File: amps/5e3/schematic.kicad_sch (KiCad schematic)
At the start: 44 parts, among them T2 8k:8

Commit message: Add: real tube pin numbers and readable valve glyphs on every schematic
Phase B of the drawing program. A factory service sheet numbers every tube
pin, because the number is what a technician puts a probe on. This corpus
printed none, and the numbers hidden in its symbols were positional
placeholders (P=1, G=2, K=3) that would have published a 6V6GT's plate as
pin 1 when it is pin 3.

1055 electrodes now carry the real number, 1027 lettered (27 are shared
filaments deduped, 1 dropped for want of clear space on the 6G2). Resolved per
instance from reference/tubes/<slug>.yaml through the same alias resolution the
layout renderer uses, so a 12AX7 section and a 6SL7 section each get their own
basing. A valve whose basing the corpus does not carry prints nothing rather
than a wrong number.

Section letters and basing units are now separate things, which cost a detour
worth recording. The RCA 12AX7-A sheet reads "Pin 1 - Plate of Unit No.2 ...
Pin 6 - Plate of Unit No.1", so unit numbering is not pin order; the 5Y3 and
GZ34 number their units in opposite pin order, so nothing positional can
express it. But the section LETTER is a designator, not a basing fact: this
corpus, like every technician, calls the first stage in signal order V1A, and
five amps' prose already did. On four amps the factory sheets put that first
stage on the other half -- the AA764's own schematic prints +200 V on pin 1 --
so those drawings now state their unit explicitly, each citing its source, and
no letter, netlist, parts list or layout comment changed. 183 layout comments
agree with the printed numbers, 0 disagree. A guard fires if two halves of one
bottle resolve to the same unit, which is exactly how this was found.

Glyphs: the cathode gains a bracket and filament hairpin so it can no longer be
confused with the plate bar, the pentode's screen sits on its own row, and a
rectifier draws as one envelope over its sections instead of two apparent
bottles. Line weights are scaled per sheet to a co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
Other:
- note added: "1"
- note added: "2"
- note added: "2,8"
- note added: "3"
- note added: "4"
- note added: "5"
- note added: "6"
- note added: "7"
- note added: "8"
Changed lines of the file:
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@@
   (wire (pts (xy 29.7916 38.278) (xy 33.6016 38.278))
     (stroke (width 0) (type default)))
-  (junction (at 29.7916 38.278) (diameter 0) (color 0 0 0 0))
+  (junction (at 29.7916 38.278) (diameter 1) (color 0 0 0 0))
   (symbol (lib_id "cx:R") (at 29.7916 42.088 0) (unit 1)
     (in_bom yes) (on_board yes)
@@
   (wire (pts (xy 29.7916 70.278) (xy 33.6016 70.278))
     (stroke (width 0) (type default)))
-  (junction (at 29.7916 70.278) (diameter 0) (color 0 0 0 0))
+  (junction (at 29.7916 70.278) (diameter 1) (color 0 0 0 0))
   (symbol (lib_id "cx:R") (at 29.7916 74.088 0) (unit 1)
     (in_bom yes) (on_board yes)
@@
   (wire (pts (xy 48.8416 80.278) (xy 48.8416 83.278))
     (stroke (width 0) (type default)))
-  (junction (at 48.8416 80.278) (diameter 0) (color 0 0 0 0))
+  (junction (at 48.8416 80.278) (diameter 1) (color 0 0 0 0))
   (symbol (lib_id "cx:R") (at 48.8416 87.088 0) (unit 1)
     (in_bom yes) (on_board yes)
@@
   (wire (pts (xy 41.2216 30.658) (xy 53.9216 30.658))
     (stroke (width 0) (type default)))
-  (junction (at 41.2216 30.658) (diameter 0) (color 0 0 0 0))
+  (junction (at 41.2216 30.658) (diameter 1) (color 0 0 0 0))
   (symbol (lib_id "cx:C") (at 57.7316 30.658 90) (unit 1)
     (in_bom yes) (on_board yes)
@@
   (wire (pts (xy 41.2216 62.658) (xy 53.9216 62.658))
     (stroke (width 0) (type default)))
-  (junction (at 41.2216 62.658) (diameter 0) (color 0 0 0 0))
+  (junction (at 41.2216 62.658) (diameter 1) (color 0 0 0 0))
   (symbol (lib_id "cx:C") (at 57.7316 62.658 90) (unit 1)
     (in_bom yes) (on_board yes)
@@
   (wire (pts (xy 74.2416 66.468) (xy 74.2416 50.278))
     (stroke (width 0) (type default)))
-  (junction (at 74.2416 50.278) (diameter 0) (color 0 0 0 0))
+  (junction (at 74.2416 50.278) (diameter 1) (color 0 0 0 0))
   (symbol (lib_id "cx:TRIODE") (at 84.4016 50.278 0) (unit 1)
     (in_bom yes) (on_board yes)
@@
   (wire (pts (xy 84.4016 42.658) (xy 94.5616 42.658))
     (stroke (width 0) (type default)))
-  (junction (at 84.4016 42.658) (diameter 0) (color 0 0 0 0))
+  (junction (at 84.4016 42.658) (diameter 1) (color 0 0 0 0))
   (wire (pts (xy 94.5616 42.658) (xy 94.5616 35.178))
     (stroke (width 0) (type default)))
@@
     (property "Reference" "RKA" (at 128.512 64.808 0) (effects (font (size 1.27 1.27)) (justify left)))
     (property "Value" "1.5k" (at 128.512 67.208 0) (effects (font (size 1.27 1.27)) (justify left))))
-  (junction (at 126.312 71.818) (diameter 0) (color 0 0 0 0))
+  (junction (at 126.312 71.818) (diameter 1) (color 0 0 0 0))
   (symbol (lib_id "cx:R") (at 126.312 75.628 0) (unit 1)
     (in_bom yes) (on_board yes)
@@
   (wire (pts (xy 116.152 54.278) (xy 116.152 64.198))
     (stroke (width 0) (type default)))
-  (junction (at 116.152 54.278) (diameter 0) (color 0 0 0 0))
+  (junction (at 116.152 54.278) (diameter 1) (color 0 0 0 0))
   (symbol (lib_id "cx:R") (at 116.152 68.008 0) (unit 1)
     (in_bom yes) (on_board yes)
@@
   (wire (pts (xy 126.312 46.658) (xy 133.932 46.658))
     (stroke (width 0) (type default)))
-  (junction (at 126.312 46.658) (diameter 0) (color 0 0 0 0))
+  (junction (at 126.312 46.658) (diameter 1) (color 0 0 0 0))
   (wire (pts (xy 141.552 46.658) (xy 142.882 46.658))
     (stroke (width 0) (type default)))
@@
   (wire (pts (xy 155.522 34.278) (xy 155.522 34.278))
     (stroke (width 0) (type default)))
-  (junction (at 146.632 34.278) (diameter 0) (color 0 0 0 0))
+  (junction (at 146.632 34.278) (diameter 1) (color 0 0 0 0))
   (symbol (lib_id "cx:R") (at 146.632 38.088 0) (unit 1)
     (in_bom yes) (on_board yes)
@@
   (wire (pts (xy 155.522 74.278) (xy 155.522 74.278))
     (stroke (width 0) (type default)))
-  (junction (at 146.632 74.278) (diameter 0) (color 0 0 0 0))
+  (junction (at 146.632 74.278) (diameter 1) (color 0 0 0 0))
   (symbol (lib_id "cx:R") (at 146.632 78.088 0) (unit 1)
     (in_bom yes) (on_board yes)
@@
   (wire (pts (xy 179.652 84.278) (xy 179.652 88.278))
     (stroke (width 0) (type default)))
-  (junction (at 179.652 84.278) (diameter 0) (color 0 0 0 0))
+  (junction (at 179.652 84.278) (diameter 1) (color 0 0 0 0))
   (symbol (lib_id "cx:R") (at 179.652 92.088 0) (unit 1)
     (in_bom yes) (on_board yes)
@@
   (wire (pts (xy 59.0016 120.078) (xy 78.0516 120.078))
     (stroke (width 0) (type default)))
-  (junction (at 46.3016 120.078) (diameter 0) (color 0 0 0 0))
-  (junction (at 59.0016 120.078) (diameter 0) (color 0 0 0 0))
+  (junction (at 46.3016 120.078) (diameter 1) (color 0 0 0 0))
+  (junction (at 59.0016 120.078) (diameter 1) (color 0 0 0 0))
   (symbol (lib_id "cx:C") (at 59.0016 123.888 0) (unit 1)
     (in_bom yes) (on_board yes)
@@
   (wire (pts (xy 94.5616 120.078) (xy 97.1016 120.078))
     (stroke (width 0) (type default)))
-  (junction (at 90.7516 120.078) (diameter 0) (color 0 0 0 0))
+  (junction (at 90.7516 120.078) (diameter 1) (color 0 0 0 0))
   (global_label "B+2" (shape input) (at 90.7516 117.538 90)
     (effects (font (size 1.27 1.27)) (justify left)))
   (wire (pts (xy 90.7516 117.538) (xy 90.7516 120.078))
     (stroke (width 0) (type default)))
-  (junction (at 94.5616 120.078) (diameter 0) (color 0 0 0 0))
+  (junction (at 94.5616 120.078) (diameter 1) (color 0 0 0 0))
   (symbol (lib_id "cx:C") (at 94.5616 123.888 0) (unit 1)
     (in_bom yes) (on_board yes)
@@
   (wire (pts (xy 107.262 120.078) (xy 112.342 120.078))
     (stroke (width 0) (type default)))
-  (junction (at 107.262 120.078) (diameter 0) (color 0 0 0 0))
+  (junction (at 107.262 120.078) (diameter 1) (color 0 0 0 0))
   (global_label "B+3" (shape input) (at 107.262 117.538 90)
     (effects (font (size 1.27 1.27)) (justify left)))
@@
   (global_label "GND" (shape input) (at 112.342 127.698 270)
     (effects (font (size 1.27 1.27)) (justify right)))
+  (polyline (pts (xy 46.3016 104.978) (xy 47.2926 105.076) (xy 48.2456 105.365) (xy 49.1236 105.834) (xy 49.8936 106.466) (xy 50.5256 107.236) (xy 50.9946 108.114) (xy 51.2836 109.067) (xy 51.3816 110.058) (xy 51.2836 111.049) (xy 50.9946 112.002) (xy 50.5256 112.88) (xy 49.8936 113.65) (xy 49.1236 114.282) (xy 48.2456 114.751) (xy 47.2926 115.04) (xy 46.3016 115.138) (xy 33.6016 115.138) (xy 32.6106 115.04) (xy 31.6576 114.751) (xy 30.7796 114.282) (xy 30.0096 113.65) (xy 29.3776 112.88) (xy 28.9086 112.002) (xy 28.6196 111.049) (xy 28.5216 110.058) (xy 28.6196 109.067) (xy 28.9086 108.114) (xy 29.3776 107.236) (xy 30.0096 106.466) (xy 30.7796 105.834) (xy 31.6576 105.365) (xy 32.6106 105.076) (xy 33.6016 104.978) (xy 46.3016 104.978))
+    (stroke (width 0.3) (type default) (color 197 163 255 1)) (fill (type none)))
+  (polyline (pts (xy 31.7016 112.293) (xy 33.6016 110.693) (xy 39.9516 112.773) (xy 46.3016 110.693) (xy 48.2016 112.293))
+    (stroke (width 0.3) (type default) (color 197 163 255 1)) (fill (type none)))
+  (text "6" (at 42.0716 31.928 0)
+    (effects (font (size 1.1 1.1)) (justify left)))
+  (text "7" (at 34.2744 36.878 0)
+    (effects (font (size 1.1 1.1)) (justify left)))
+  (text "8" (at 43.5216 44.628 0)
+    (effects (font (size 1.1 1.1)) (justify left)))
+  (text "1" (at 42.0716 63.928 0)
+    (effects (font (size 1.1 1.1)) (justify left)))
+  (text "2" (at 34.2744 68.878 0)
+    (effects (font (size 1.1 1.1)) (justify left)))
+  (text "3" (at 42.0716 76.628 0)
+    (effects (font (size 1.1 1.1)) (justify left)))
+  (text "6" (at 85.2516 43.928 0)
+    (effects (font (size 1.1 1.1)) (justify left)))
+  (text "7" (at 77.4544 48.878 0)
+    (effects (font (size 1.1 1.1)) (justify left)))
+  (text "8" (at 85.2516 56.628 0)
+    (effects (font (size 1.1 1.1)) (justify left)))
+  (text "1" (at 127.162 47.928 0)
+    (effects (font (size 1.1 1.1)) (justify left)))
+  (text "2" (at 119.364 52.878 0)
+    (effects (font (size 1.1 1.1)) (justify left)))
+  (text "3" (at 127.162 60.628 0)
+    (effects (font (size 1.1 1.1)) (justify left)))
+  (text "3" (at 163.992 27.293 0)
+    (effects (font (size 1.1 1.1)) (justify left)))
+  (text "5" (at 156.194 32.878 0)
+    (effects (font (size 1.1 1.1)) (justify left)))
+  (text "4" (at 169.042 31.608 0)
+    (effects (font (size 1.1 1.1)) (justify left)))
+  (text "8" (at 163.992 39.993 0)
+    (effects (font (size 1.1 1.1)) (justify left)))
+  (text "3" (at 163.992 67.293 0)
+    (effects (font (size 1.1 1.1)) (justify left)))
+  (text "5" (at 156.194 72.878 0)
+    (effects (font (size 1.1 1.1)) (justify left)))
+  (text "4" (at 169.042 71.608 0)
+    (effects (font (size 1.1 1.1)) (justify left)))
+  (text "8" (at 163.992 79.993 0)
+    (effects (font (size 1.1 1.1)) (justify left)))
+  (text "6" (at 34.4516 103.708 0)
+    (effects (font (size 1.1 1.1)) (justify left)))
+  (text "2,8" (at 34.4516 116.408 0)
+    (effects (font (size 1.1 1.1)) (justify left)))
+  (text "4" (at 47.1516 103.708 0)
+    (effects (font (size 1.1 1.1)) (justify left)))
   (text "Heaters and PT primary omitted — see netlist.cir and meta.yaml" (at 12.7 138.856 0)
     (effects (font (size 1.2 1.2)) (justify left)))

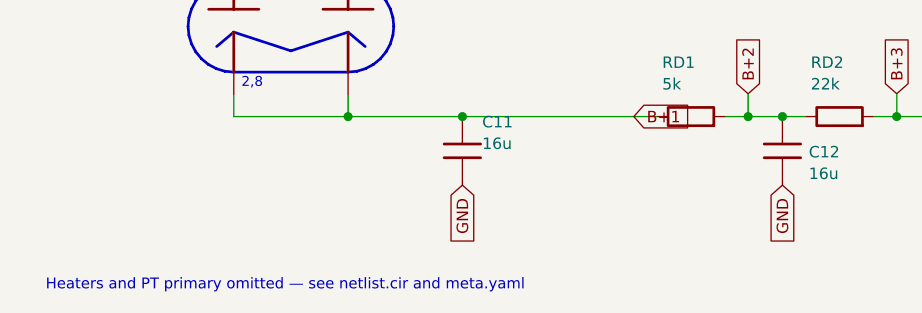
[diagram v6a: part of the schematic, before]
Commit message: Fix: schematic sheet notes no longer name repository files
Thirty-seven committed sheets rendered footnotes and section notes such as
"Heaters and PT primary omitted — see netlist.cir and meta.yaml" or
"excluded from netlist.cir (notes.md)" to visitors through KiCanvas. The
prose sweeps never counted sheets. Rewritten in the site's own words — the
netlist, the sources list, the circuit story, the parts list, the board
drawing — in 59 strings across 33 draw scripts, keeping every technical
claim as it was; the three tone sheets (6G4, 6G5, 6G6-B) are under repair
elsewhere and keep theirs for now. The sweep touched only strings passed to
the sheet's note, text, caption and footnote calls, never a path or a value.

Gates: check_schematics 40/0, connectivity 0 isolated pins;
verify_schematic_nets 40 clean; only the regenerated sheets and their served
copies changed.

Co-Authored-By: Claude Fable 5.1 <noreply@anthropic.com>
Claude-Session: https://claude.ai/code/session_01KBMfdh37HmCL2iWcBiL5J1
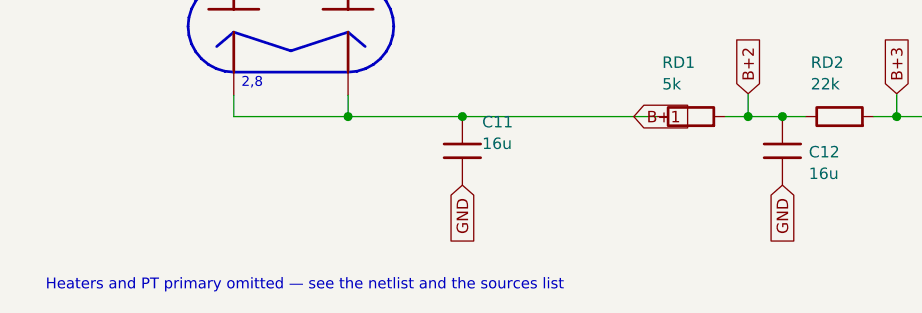
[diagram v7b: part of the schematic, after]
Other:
- note added: "Heaters and PT primary omitted — see the netlist and the sources list"
- note removed: "Heaters and PT primary omitted — see netlist.cir and meta.yaml"
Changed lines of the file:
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@@
   (text "4" (at 47.1516 103.708 0)
     (effects (font (size 1.1 1.1)) (justify left)))
-  (text "Heaters and PT primary omitted — see netlist.cir and meta.yaml" (at 12.7 138.856 0)
+  (text "Heaters and PT primary omitted — see the netlist and the sources list" (at 12.7 138.856 0)
     (effects (font (size 1.2 1.2)) (justify left)))
   (sheet_instances (path "/" (page "1")))

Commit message: Fix: 5E3 cathodyne's lower coupler taken off the cathode, as F-EE draws it
- F-EE schematic (6118 x 3617, crop (2991,1088)-(3900,2250)): the .1-200
  leaves the dot above the 1500 -- the cathode; the 1500/56K junction carries
  only the 1 MEG return. F-EE layout (6361 x 3988, crop (3322,1661)-(4736,3640)):
  the cap's lower eyelet takes the 1500's cathode end.
- Netlist C8 JPI -> KPI; sheet tap moved to RKA's top; board run RKA.b -> C8.a
  becomes RKA.a -> C8.a; notes say where the coupler sits. DC-open, so no
  operating point moves.
- History: a280d58 (2026-07-19) put C8 on JPI, "the balanced 1.5k/56k junction
  ... confirmed by the equivalence checker" -- which can only confirm that a
  drawing agrees with the netlist. The sheet tapped the cathode until 11e9875
  (2026-09-02) moved it to the junction to clear a verify_schematic_nets
  finding against that netlist, leaving the comment "It used to be taken off the
  cathode pin itself". The netlist was the misreading.
- Gates: verify_schematic_nets 5e3 PASS (CLAIMED); verify_layout_nets 5e3 PASS
  (claimed); lint clean both styles.

Co-Authored-By: Claude Opus 5 (1M context) <noreply@anthropic.com>
Claude-Session: https://claude.ai/code/session_01KBMfdh37HmCL2iWcBiL5J1
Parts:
- removed RK66: 250 5W, symbol cx:R
- added C9: 25u, symbol cx:C
- RK66: renamed from C9; value 25u -> 250 5W; symbol cx:C -> cx:R
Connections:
- net GND: now also C9.2
- net at RK66.1, V3.4 (K), V4.4 (K): now also C9.1
- net at RGPI.2, RKA.2, RKB.1: no longer C8.1
- net at RKA.1, V2B.3 (K): now also C8.1
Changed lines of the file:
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@@
   (wire (pts (xy 142.882 46.658) (xy 142.882 34.278))
     (stroke (width 0) (type default)))
-  (wire (pts (xy 126.312 71.818) (xy 133.932 71.818))
+  (junction (at 126.312 64.198) (diameter 1) (color 0 0 0 0))
+  (wire (pts (xy 126.312 64.198) (xy 133.932 64.198))
     (stroke (width 0) (type default)))
-  (symbol (lib_id "cx:C") (at 137.742 71.818 90) (unit 1)
+  (symbol (lib_id "cx:C") (at 137.742 64.198 90) (unit 1)
     (in_bom yes) (on_board yes)
-    (property "Reference" "C8" (at 134.542 65.618 270) (effects (font (size 1.27 1.27)) (justify left)))
-    (property "Value" ".1u" (at 134.542 68.018 270) (effects (font (size 1.27 1.27)) (justify left))))
-  (wire (pts (xy 141.552 71.818) (xy 142.882 71.818))
+    (property "Reference" "C8" (at 134.542 57.998 270) (effects (font (size 1.27 1.27)) (justify left)))
+    (property "Value" ".1u" (at 134.542 60.398 270) (effects (font (size 1.27 1.27)) (justify left))))
+  (wire (pts (xy 141.552 64.198) (xy 142.882 64.198))
     (stroke (width 0) (type default)))
-  (wire (pts (xy 142.882 71.818) (xy 142.882 74.278))
+  (wire (pts (xy 142.882 64.198) (xy 142.882 74.278))
     (stroke (width 0) (type default)))
   (symbol (lib_id "cx:R") (at 151.712 34.278 90) (unit 1)
